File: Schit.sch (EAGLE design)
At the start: 15 parts, among them IC2 MEGA16-A, Q1 12M

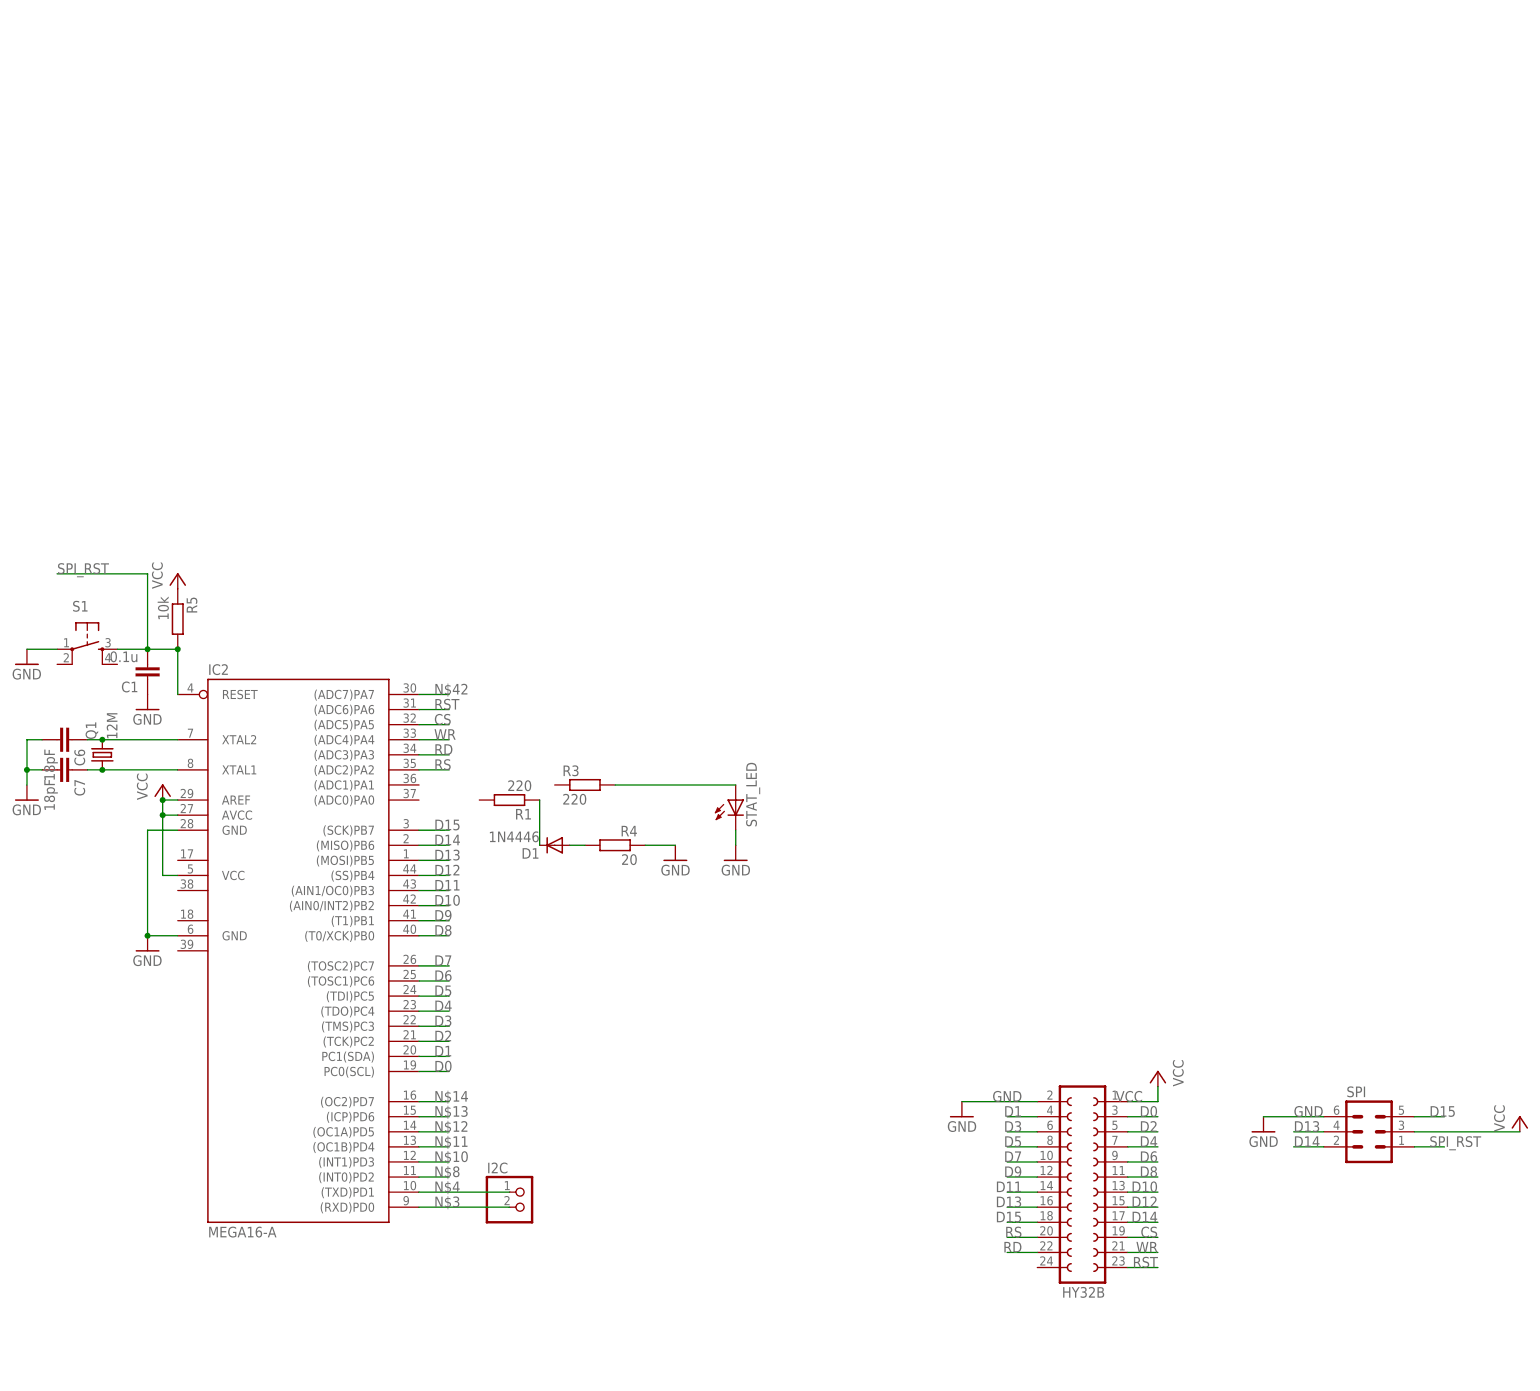
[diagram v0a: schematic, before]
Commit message: change mc to ATMega64A
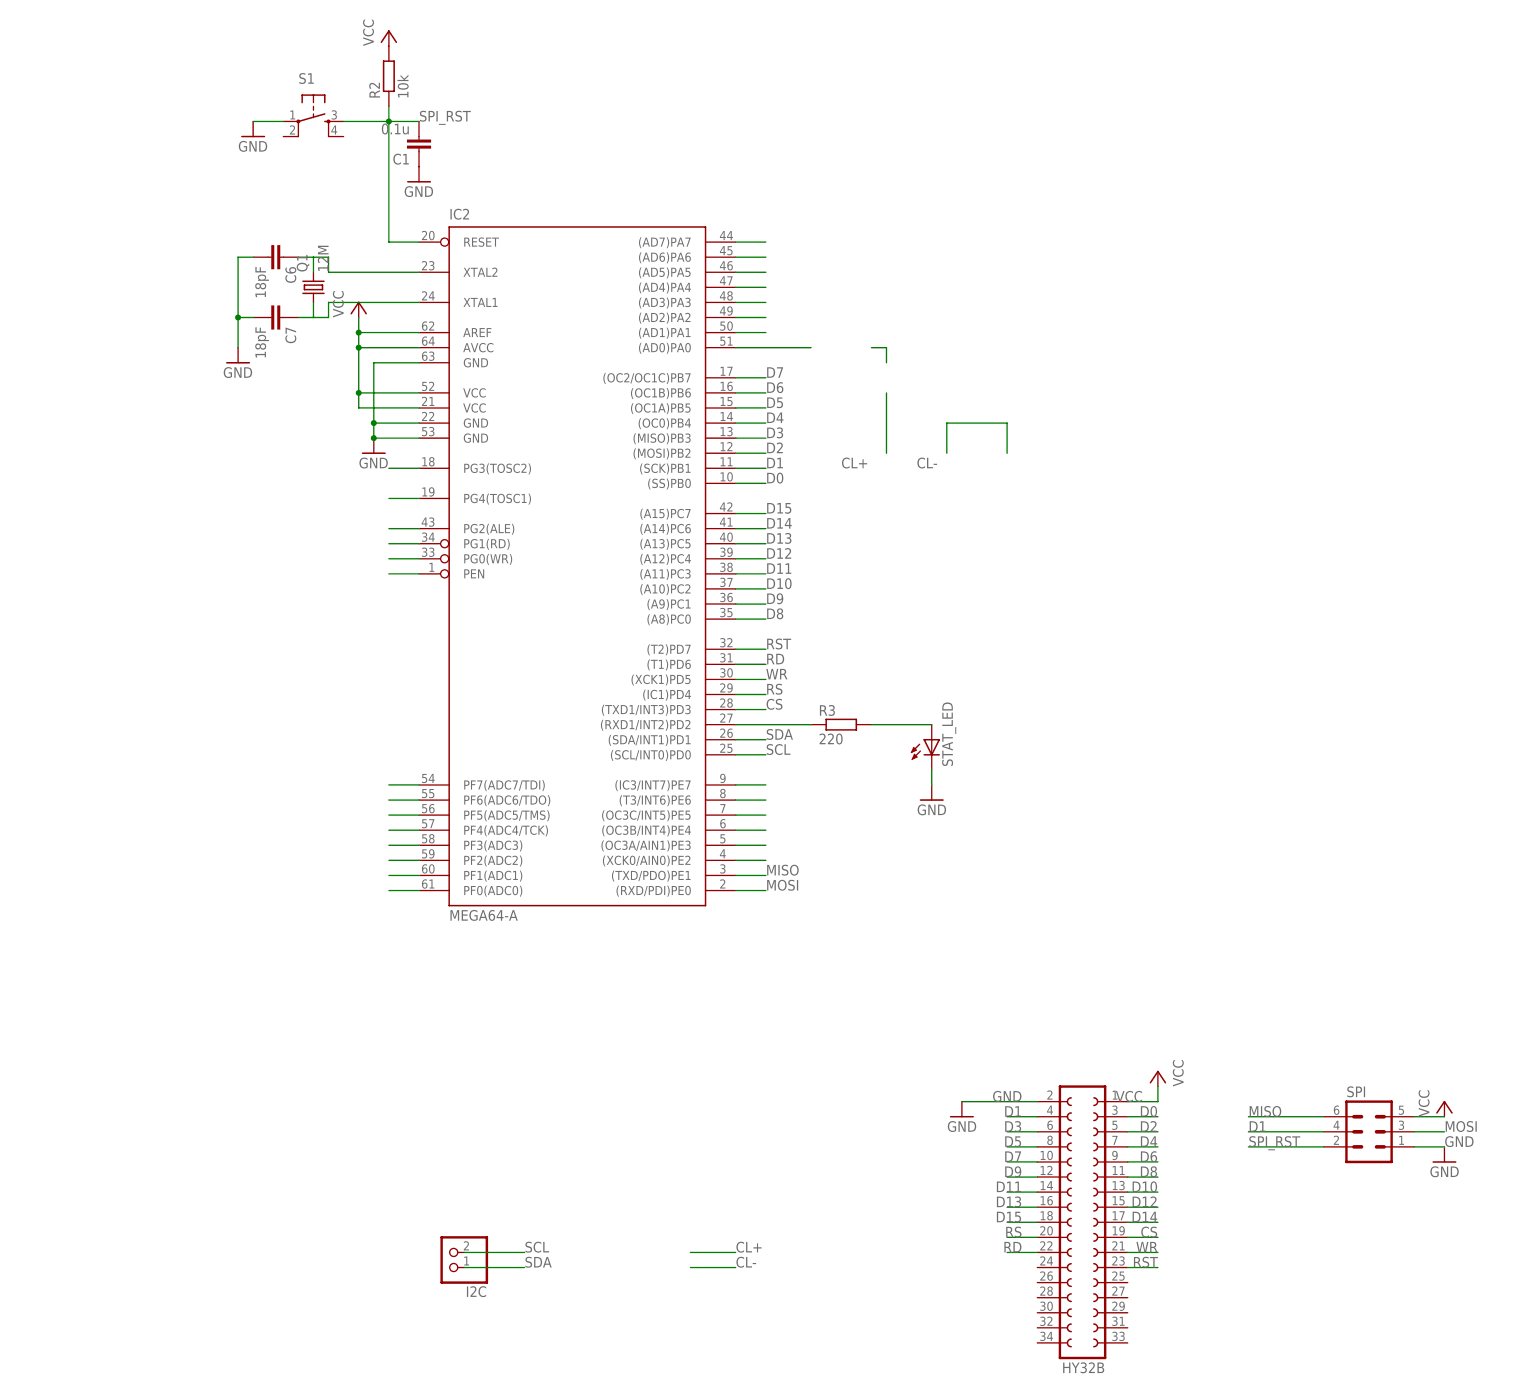
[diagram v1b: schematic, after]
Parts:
- removed D1: 1N4446, diode:1N4446
- removed R1: 220, resistor:R-EU_R1206
- removed R4: 20, resistor:R-EU_R1206
- removed R5: 10k, rcl:R-EU_R0805
- added R2: 10k, rcl:R-EU_R0805
- HY32B: device con-lsta:FE12-2 -> con-lsta:FE17-2
- IC2: value MEGA16-A -> MEGA64-A; device atmel:MEGA16-A -> atmel:MEGA64-A
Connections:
- net XTAL1 renamed N$30
- removed net N$10: IC2.(INT1)PD3
- removed net N$11: IC2.(OC1B)PD4
- removed net N$12: IC2.(OC1A)PD5
- removed net N$13: IC2.(ICP)PD6
- removed net N$14: IC2.(OC2)PD7
- removed net N$2: D1.A, R4.2
- removed net N$3: I2C.2, IC2.(RXD)PD0
- removed net N$4: I2C.1, IC2.(TXD)PD1
- removed net N$42: IC2.(ADC7)PA7
- removed net N$8: IC2.(INT0)PD2
- new net MISO: IC2.(TXD/PDO)PE1, SPI.6
- new net MOSI: IC2.(RXD/PDI)PE0, SPI.3
- new net N$23: IC2.(XCK0/AIN0)PE2
- new net N$24: IC2.(OC3A/AIN1)PE3
- new net N$25: IC2.(OC3B/INT4)PE4
- new net N$26: IC2.(OC3C/INT5)PE5
- new net N$27: IC2.(T3/INT6)PE6
- new net N$28: IC2.(IC3/INT7)PE7
- new net N$54: IC2.(AD0)PA0
- new net N$55: IC2.(AD1)PA1
- new net N$56: IC2.(AD2)PA2
- new net N$57: IC2.(AD3)PA3
- new net N$58: IC2.(AD4)PA4
- new net N$59: IC2.(AD5)PA5
- new net N$60: IC2.(AD6)PA6
- new net N$61: IC2.(AD7)PA7
- new net N$72: IC2.PG3(TOSC2)
- new net N$73: IC2.PG4(TOSC1)
- new net N$74: IC2.PG2(ALE)
- new net N$75: IC2.PG1(RD)
- new net N$76: IC2.PG0(WR)
- new net N$77: IC2.PEN
- new net N$78: IC2.PF7(ADC7/TDI)
- new net N$79: IC2.PF6(ADC6/TDO)
- new net N$80: IC2.PF5(ADC5/TMS)
- new net N$81: IC2.PF4(ADC4/TCK)
- new net N$82: IC2.PF3(ADC3)
- new net N$83: IC2.PF2(ADC2)
- new net N$84: IC2.PF1(ADC1)
- new net N$85: IC2.PF0(ADC0)
- new net SCL: I2C.2, IC2.(SCL/INT0)PD0
- new net SDA: I2C.1, IC2.(SDA/INT1)PD1
- net CS: now also IC2.(TXD1/INT3)PD3; no longer IC2.(ADC5)PA5
- net D0: now also IC2.(SS)PB0; no longer IC2.PC0(SCL)
- net D1: now also IC2.(SCK)PB1, SPI.4; no longer IC2.PC1(SDA)
- net D10: now also IC2.(A10)PC2; no longer IC2.(AIN0/INT2)PB2
- net D11: now also IC2.(A11)PC3; no longer IC2.(AIN1/OC0)PB3
- net D12: now also IC2.(A12)PC4; no longer IC2.(SS)PB4
- net D13: now also IC2.(A13)PC5; no longer IC2.(MOSI)PB5, SPI.4
- net D14: now also IC2.(A14)PC6; no longer IC2.(MISO)PB6, SPI.2
- net D15: now also IC2.(A15)PC7; no longer IC2.(SCK)PB7, SPI.5
- net D2: now also IC2.(MOSI)PB2; no longer IC2.(TCK)PC2
- net D3: now also IC2.(MISO)PB3; no longer IC2.(TMS)PC3
- net D4: now also IC2.(OC0)PB4; no longer IC2.(TDO)PC4
- net D5: now also IC2.(OC1A)PB5; no longer IC2.(TDI)PC5
- net D6: now also IC2.(OC1B)PB6; no longer IC2.(TOSC1)PC6
- net D7: now also IC2.(OC2/OC1C)PB7; no longer IC2.(TOSC2)PC7
- net D8: now also IC2.(A8)PC0; no longer IC2.(T0/XCK)PB0
- net D9: now also IC2.(A9)PC1; no longer IC2.(T1)PB1
- net GND: now also IC2.GND@2, SPI.1; no longer R4.1, SPI.6
- net N$1: now also IC2.(RXD1/INT2)PD2, R3.1; no longer D1.C, R1.1
- net RD: now also IC2.(T1)PD6; no longer IC2.(ADC3)PA3
- net RS: now also IC2.(IC1)PD4; no longer IC2.(ADC2)PA2
- net RST: now also IC2.(T2)PD7; no longer IC2.(ADC6)PA6
- net SPI_RST: now also R2.1, SPI.2; no longer R5.2, SPI.1
- net VCC: now also IC2.VCC@1, R2.2, SPI.5; no longer R5.1, SPI.3
- net WR: now also IC2.(XCK1)PD5; no longer IC2.(ADC4)PA4
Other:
- moved on the sheet: C1, C6, C7, I2C, Q1, R3, S1, STAT_LED

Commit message: change mc to ATmega128A
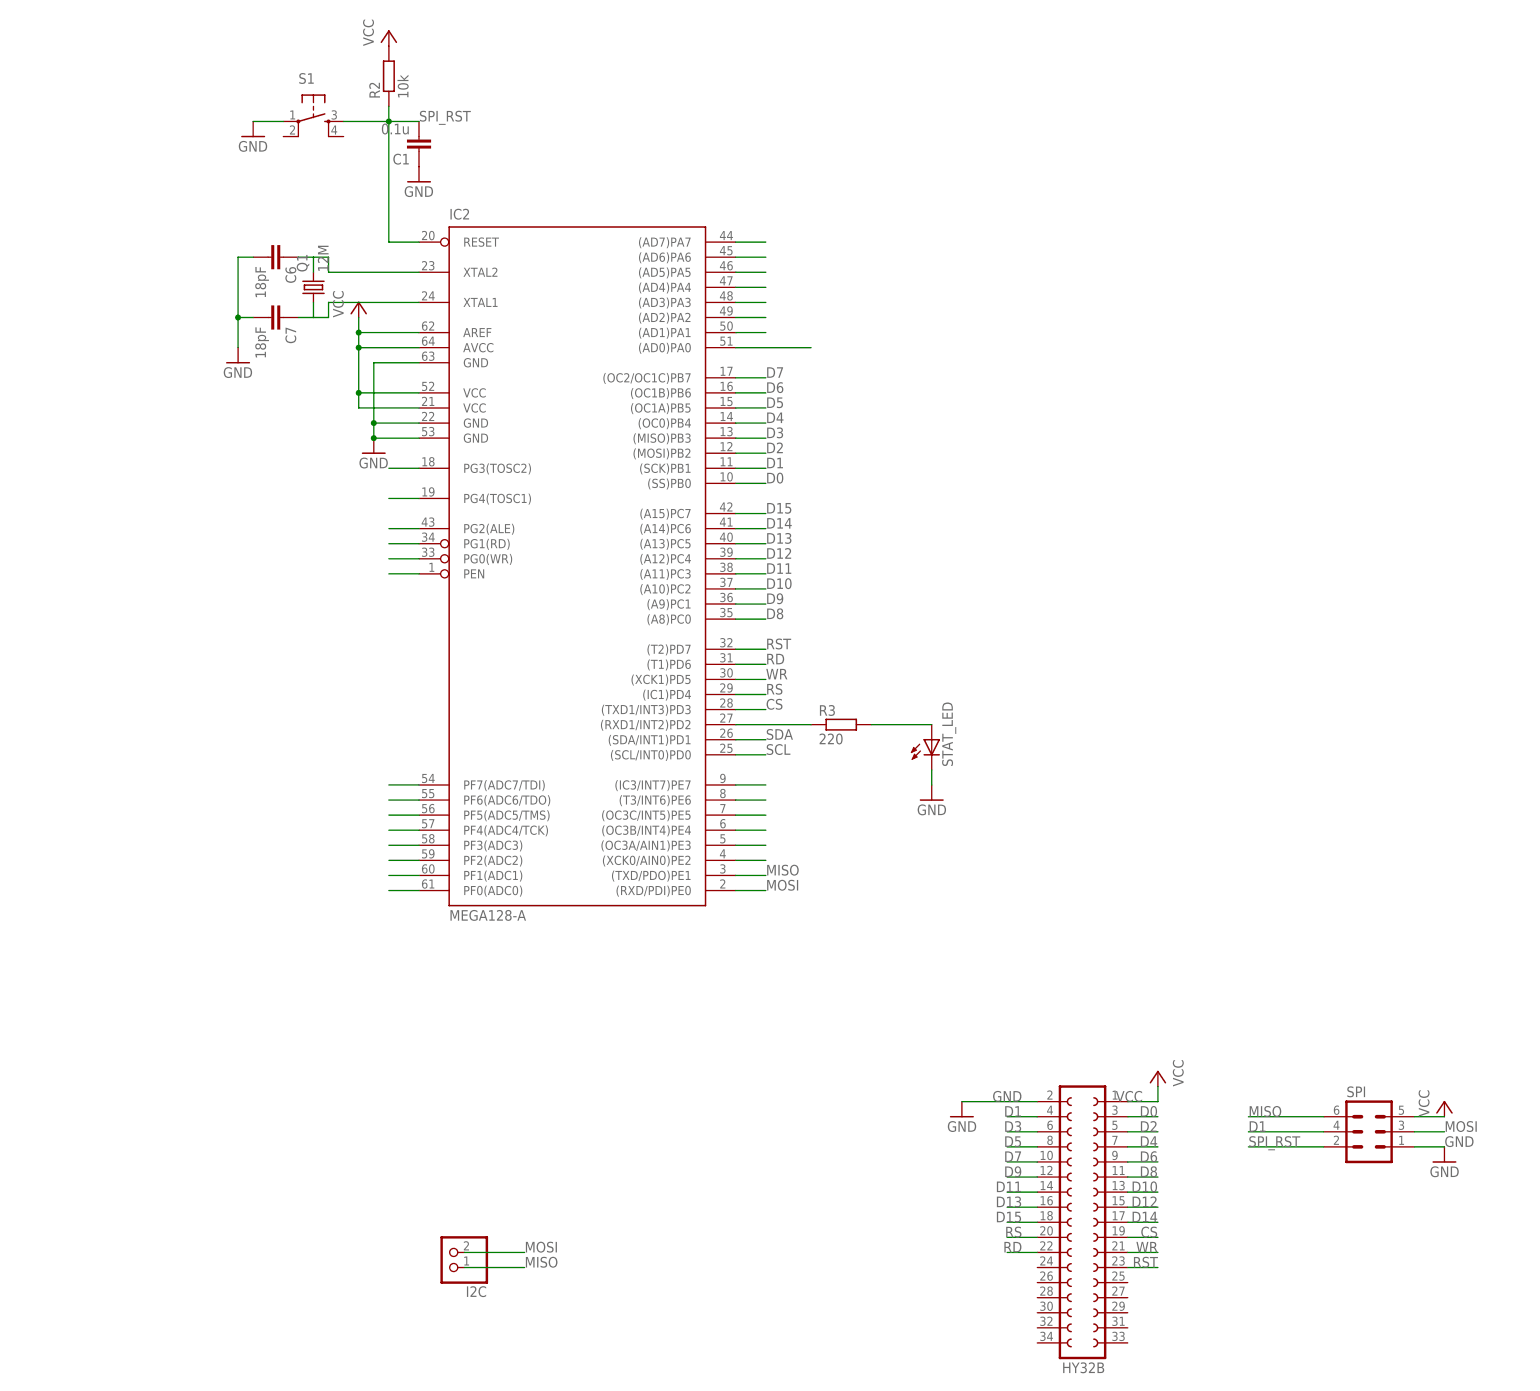
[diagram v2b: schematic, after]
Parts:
- IC2: value MEGA64-A -> MEGA128-A; device atmel:MEGA64-A -> atmel:MEGA128-A
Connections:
- net MISO: now also I2C.1
- net MOSI: now also I2C.2
- net SCL: no longer I2C.2
- net SDA: no longer I2C.1
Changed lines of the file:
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@@
 <part name="I2C" library="pinhead" deviceset="PINHD-1X2" device=""/>
 <part name="P+3" library="supply1" deviceset="VCC" device=""/>
-<part name="IC2" library="atmel" deviceset="MEGA64" device="-A"/>
+<part name="IC2" library="atmel" deviceset="MEGA128" device="-A"/>
 <part name="GND7" library="supply1" deviceset="GND" device=""/>
 <part name="C1" library="rcl" deviceset="C-EU" device="C0805" value="0.1u"/>
@@
 <instance part="I2C" gate="G$1" x="43.18" y="25.4" rot="R180"/>
 <instance part="P+3" gate="VCC" x="210.82" y="50.8"/>
-<instance part="IC2" gate="G$1" x="63.5" y="144.78"/>
+<instance part="IC2" gate="G$1" x="66.04" y="142.24"/>
 <instance part="GND7" gate="1" x="30.48" y="160.02"/>
 <instance part="C1" gate="G$1" x="38.1" y="210.82" rot="R180"/>
@@
 <net name="SCL" class="0">
 <segment>
+<pinref part="IC2" gate="G$1" pin="(SCL/INT0)PD0"/>
+<wire x1="91.44" y1="109.22" x2="96.52" y2="109.22" width="0.1524" layer="91"/>
+<label x="96.52" y="109.22" size="1.778" layer="95"/>
+</segment>
+</net>
+<net name="SDA" class="0">
+<segment>
+<pinref part="IC2" gate="G$1" pin="(SDA/INT1)PD1"/>
+<wire x1="91.44" y1="111.76" x2="96.52" y2="111.76" width="0.1524" layer="91"/>
+<label x="96.52" y="111.76" size="1.778" layer="95"/>
+</segment>
+</net>
+<net name="MOSI" class="0">
+<segment>
+<pinref part="IC2" gate="G$1" pin="(RXD/PDI)PE0"/>
+<wire x1="91.44" y1="86.36" x2="96.52" y2="86.36" width="0.1524" layer="91"/>
+<label x="96.52" y="86.36" size="1.778" layer="95"/>
+</segment>
+<segment>
+<pinref part="SPI" gate="1" pin="3"/>
+<wire x1="205.74" y1="45.72" x2="210.82" y2="45.72" width="0.1524" layer="91"/>
+<label x="210.82" y="45.72" size="1.778" layer="95"/>
+</segment>
+<segment>
 <pinref part="I2C" gate="G$1" pin="2"/>
 <wire x1="45.72" y1="25.4" x2="55.88" y2="25.4" width="0.1524" layer="91"/>
 <label x="55.88" y="25.4" size="1.778" layer="95"/>
 </segment>
-<segment>
-<pinref part="IC2" gate="G$1" pin="(SCL/INT0)PD0"/>
-<wire x1="91.44" y1="109.22" x2="96.52" y2="109.22" width="0.1524" layer="91"/>
-<label x="96.52" y="109.22" size="1.778" layer="95"/>
-</segment>
-</net>
-<net name="SDA" class="0">
+</net>
+<net name="MISO" class="0">
+<segment>
+<pinref part="IC2" gate="G$1" pin="(TXD/PDO)PE1"/>
+<wire x1="91.44" y1="88.9" x2="96.52" y2="88.9" width="0.1524" layer="91"/>
+<label x="96.52" y="88.9" size="1.778" layer="95"/>
+</segment>
+<segment>
+<pinref part="SPI" gate="1" pin="6"/>
+<wire x1="190.5" y1="48.26" x2="177.8" y2="48.26" width="0.1524" layer="91"/>
+<label x="177.8" y="48.26" size="1.778" layer="95"/>
+</segment>
 <segment>
 <pinref part="I2C" gate="G$1" pin="1"/>
 <wire x1="45.72" y1="22.86" x2="55.88" y2="22.86" width="0.1524" layer="91"/>
 <label x="55.88" y="22.86" size="1.778" layer="95"/>
-</segment>
-<segment>
-<pinref part="IC2" gate="G$1" pin="(SDA/INT1)PD1"/>
-<wire x1="91.44" y1="111.76" x2="96.52" y2="111.76" width="0.1524" layer="91"/>
-<label x="96.52" y="111.76" size="1.778" layer="95"/>
-</segment>
-</net>
-<net name="N$6" class="0">
-<segment>
-<wire x1="114.3" y1="177.8" x2="116.84" y2="177.8" width="0.1524" layer="91"/>
-<wire x1="116.84" y1="177.8" x2="116.84" y2="175.26" width="0.1524" layer="91"/>
-</segment>
-</net>
-<net name="MOSI" class="0">
-<segment>
-<pinref part="IC2" gate="G$1" pin="(RXD/PDI)PE0"/>
-<wire x1="91.44" y1="86.36" x2="96.52" y2="86.36" width="0.1524" layer="91"/>
-<label x="96.52" y="86.36" size="1.778" layer="95"/>
-</segment>
-<segment>
-<pinref part="SPI" gate="1" pin="3"/>
-<wire x1="205.74" y1="45.72" x2="210.82" y2="45.72" width="0.1524" layer="91"/>
-<label x="210.82" y="45.72" size="1.778" layer="95"/>
-</segment>
-</net>
-<net name="MISO" class="0">
-<segment>
-<pinref part="IC2" gate="G$1" pin="(TXD/PDO)PE1"/>
-<wire x1="91.44" y1="88.9" x2="96.52" y2="88.9" width="0.1524" layer="91"/>
-<label x="96.52" y="88.9" size="1.778" layer="95"/>
-</segment>
-<segment>
-<pinref part="SPI" gate="1" pin="6"/>
-<wire x1="190.5" y1="48.26" x2="177.8" y2="48.26" width="0.1524" layer="91"/>
-<label x="177.8" y="48.26" size="1.778" layer="95"/>
 </segment>
 </net>
@@
 </segment>
 </net>
-<net name="CL+" class="0">
-<segment>
-<wire x1="116.84" y1="170.18" x2="116.84" y2="160.02" width="0.1524" layer="91"/>
-<label x="109.22" y="157.48" size="1.778" layer="95"/>
-</segment>
-<segment>
-<wire x1="83.82" y1="25.4" x2="91.44" y2="25.4" width="0.1524" layer="91"/>
-<label x="91.44" y="25.4" size="1.778" layer="95"/>
-</segment>
-</net>
-<net name="CL-" class="0">
-<segment>
-<wire x1="127" y1="165.1" x2="137.16" y2="165.1" width="0.1524" layer="91"/>
-<wire x1="137.16" y1="165.1" x2="137.16" y2="160.02" width="0.1524" layer="91"/>
-<wire x1="127" y1="165.1" x2="127" y2="160.02" width="0.1524" layer="91"/>
-<label x="121.92" y="157.48" size="1.778" layer="95"/>
-</segment>
-<segment>
-<wire x1="83.82" y1="22.86" x2="91.44" y2="22.86" width="0.1524" layer="91"/>
-<label x="91.44" y="22.86" size="1.778" layer="95"/>
-</segment>
-</net>
